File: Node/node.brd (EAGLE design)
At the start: 76.2 x 44.3 mm, 96 parts, among them CN4 MicroUSB, J1 U.FL, U1 MCP73871, U2 DW1000-I, U3 TPS61090RSAR, U4 ATMEGA328, X2 332-02, Y1 8MHz

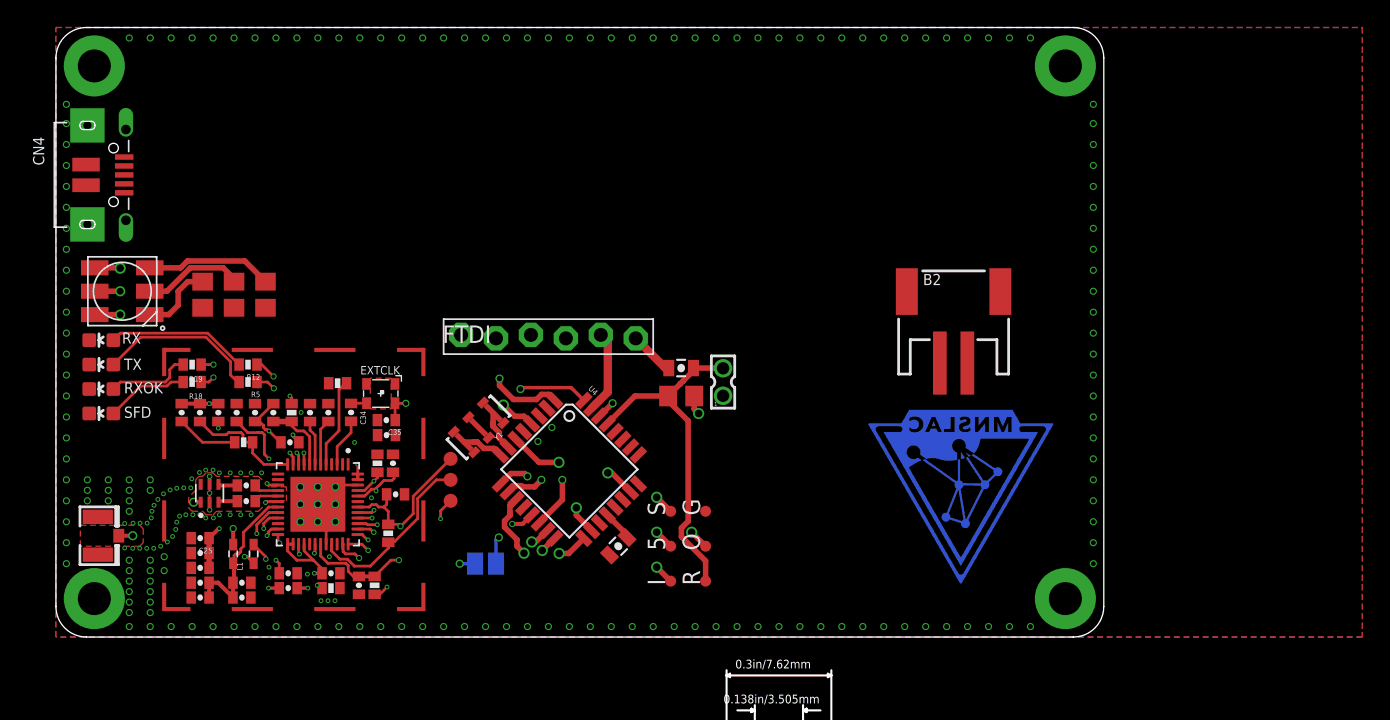
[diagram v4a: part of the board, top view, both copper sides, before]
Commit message: Added CP2105 FTDI chip
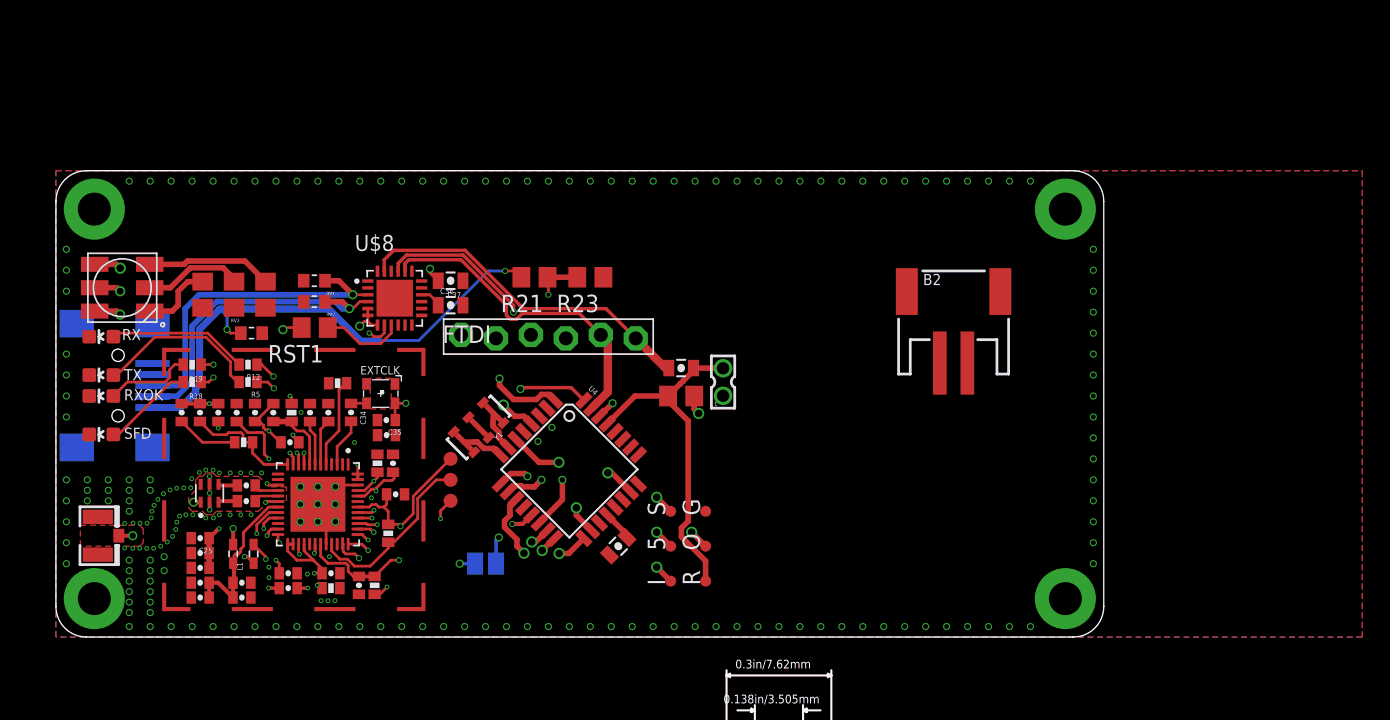
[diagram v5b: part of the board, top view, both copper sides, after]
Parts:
- removed CN4: MicroUSB, microbuilder:4UCONN_20329
- added C36: 4.7uF, SparkFun-Capacitors:0805-CAP
- added C37: 2uF, SparkFun-Capacitors:0805-CAP
- added J2: USBSMD, SparkFun-Connectors:USB-MINIB
- added R21: 24K, resistor:R0805
- added R23: 47K, resistor:R0805
- added RST1: 4.7K, resistor:R0805
- added RV1, RV2, RV3: WE-VE_0603_REFLOW, Wurth_Elektronik_Passive_rev15e:WESURGE_0603_REFLOW
- added U$8: CP2105, MainLib:QFN50P400X400X80-25N
- U$1: value MNSLAC0.25-EXP -> MNSLAC0.25; device MainLib:MNSLAC-0.25-EXPOSED -> MainLib:MNSLAC-0.25
- moved SFD 1.52 mm to (3.30, 14.7)
- moved TX 0.76 mm to (3.30, 19.1)
- moved RXOK 0.51 mm to (3.30, 17.5)
- moved RX 0.25 mm to (3.30, 21.8)
- moved LED1 0.25 mm to (4.83, 25.4)
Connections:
- new net D+: J2.D+, RV1.1, U$8.3
- new net D-: J2.D-, RV2.1, U$8.4
- new net N$19: RST1.1, U$8.9
- new net N$28: R21.1, R23.2, U$8.8
- new net N$29: C36.1, U$8.16
- net 3.3V: now also C37.2, RST1.2, U$8.5, U$8.6, U$8.7
- net DTR: now also U$8.23
- net GND: now also C36.2, C37.1, J2.GND, R23.1, RV1.2, RV2.2, RV3.2, U$8.2, U$8.25; no longer CN4.BASE@1, CN4.BASE@2, CN4.GND, CN4.SPRT@1, CN4.SPRT@2, CN4.SPRT@3, CN4.SPRT@4
- net RXD: now also U$8.21
- net TXD: now also U$8.20
- net VBUS: now also J2.VBUS, R21.2, RV3.1; no longer CN4.VBUS
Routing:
- net VBUS: track 0.00 -> 38.5 mm, vias 0 -> 2
- net D+: track 0.00 -> 23.8 mm, vias 0 -> 1
- net D-: track 0.00 -> 23.3 mm, vias 0 -> 1
- net DTR: track 3.30 -> 25.4 mm
- net N$28: track 0.00 -> 19.5 mm, vias 0 -> 2
- net TXD: track 6.03 -> 24.0 mm
- net RXD: track 8.57 -> 24.9 mm, vias 1 -> 2
- net N$19: track 0.00 -> 6.00 mm
- net 3.3V: track 25.0 -> 30.0 mm, vias 12 -> 15
- net N$29: track 0.00 -> 1.61 mm
- net N$21: track 6.02 -> 6.66 mm
- net GND: vias 232 -> 214
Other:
- board size 76.2 x 44.3 mm -> 76.2 x 33.9 mm

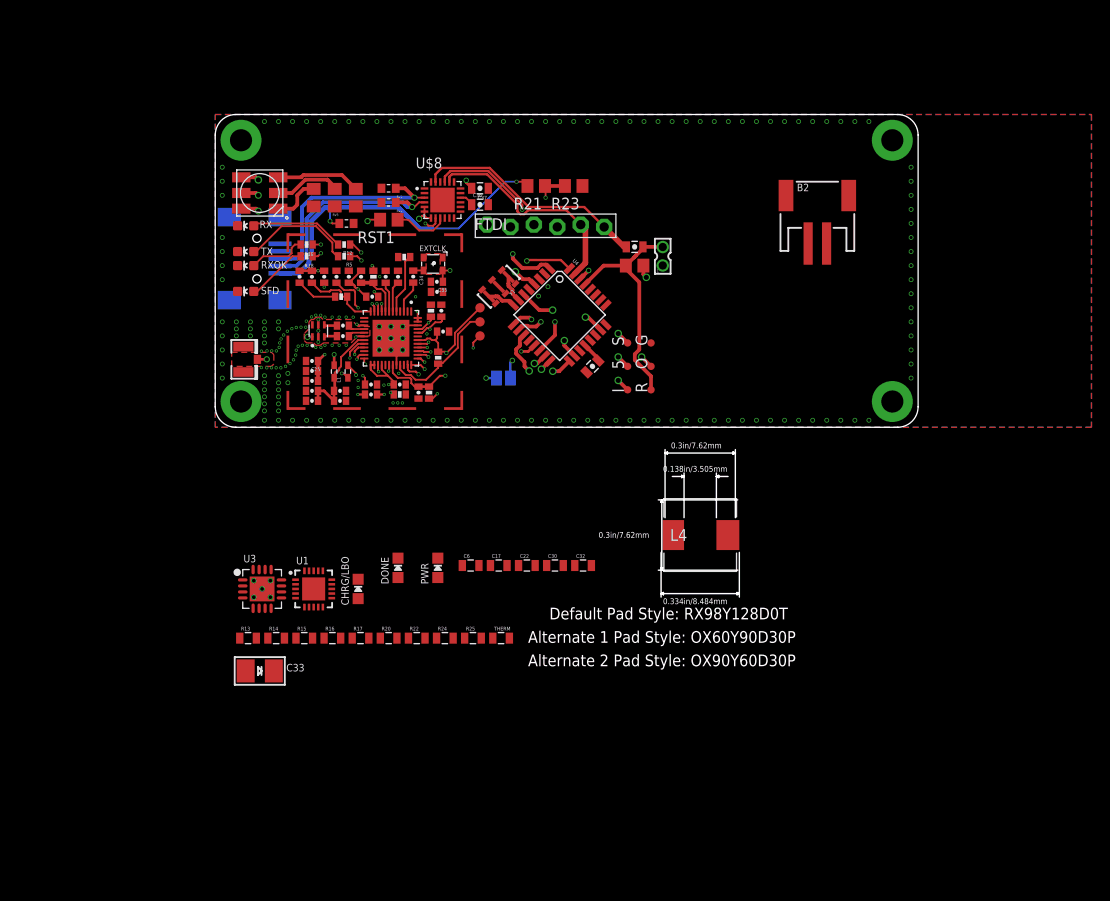
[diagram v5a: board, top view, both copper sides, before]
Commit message: Added sram chip, compass, buck/boost converter, lipo charger. DRC checks. Cosmetic changes.
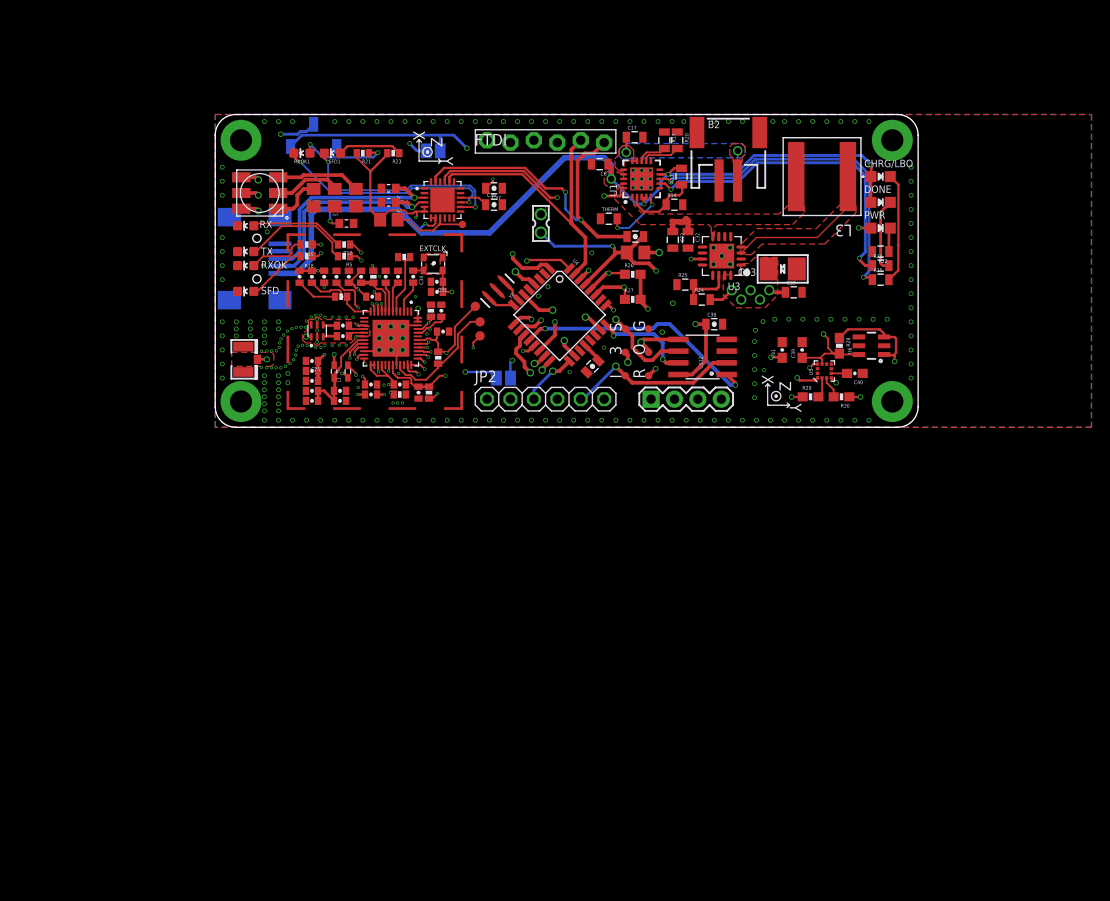
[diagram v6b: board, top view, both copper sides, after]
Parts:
- removed 5: TPSQTP08R, testpad:TP08R
- removed L4: https://www.digikey.com/product-detail/en/eaton-electronics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, MainLib:DR73
- removed Y1: 8MHz, SparkFun-FreqCtrl:RESONATOR-SMD_MED
- added 3, CPRST: TPSQTP08R, testpad:TP08R
- added C38: 1uF, SparkFun-Capacitors:0805-CAP
- added C39, C40, C41: 0.1uF, SparkFun-Capacitors:0603-CAP
- added JP1: (no value), SparkFun-Connectors:1X04
- added JP2: (no value), adafruit:1X06
- added L3: NR8040T6R8N, MainLib:IND_TAIYO_NR8040
- added R26, R27: 4.7K, SparkFun-Resistors:0603-RES
- added R28: 68, SparkFun-Passives:0603-RES
- added R29, R30: 10K, SparkFun-Resistors:0603-RES
- added RXOK1, SFD1: (no value), SparkFun-LED:LED-0603
- added SJ2: (no value), jumper:SJ
- added TP3: VDD_TP, SparkFun-Passives:TP_15TH
- added U$12: 23A640, MainLib:SOIC-8
- added U$15: SWITCH_SPDTJS102011JCQN, MainLib:JS102011JCQN
- added U5: LSM303C, SparkFun-DigitalIC:LGA-12
- added U6: LM3880, SparkFun-DigitalIC:SOT23-6
- added Y2: 8MHZ, SparkFun-FreqCtrl:RESONATOR-SMD
- R21: value 24K -> 470; device resistor:R0805 -> SparkFun-Passives:0402-RES
- R23: value 47K -> 470; device resistor:R0805 -> SparkFun-Passives:0402-RES
- moved R15 73.6 mm to (72.1, 16.0)
- moved CHRG/LBO 72.2 mm to (72.1, 27.2), turned to 270 degrees
- moved R16 71.9 mm to (72.1, 17.5)
- moved C33 71.5 mm to (61.5, 17.2), turned to 180 degrees
- moved R13 68.6 mm to (50.5, 27.2), turned to 90 degrees
- moved DONE 65.6 mm to (72.1, 24.4), turned to 270 degrees
- moved R22 65.5 mm to (72.1, 19.1), turned to 180 degrees
- moved R14 63.8 mm to (49.8, 24.1)
- moved R17 63.2 mm to (48.7, 31.1), turned to 270 degrees
- moved R20 62.4 mm to (50.1, 31.1), turned to 270 degrees
- moved U3 61.5 mm to (54.9, 18.6), turned to 180 degrees
- moved PWR 60.5 mm to (72.1, 21.6), turned to 270 degrees
- moved U1 56.9 mm to (46.2, 26.9), turned to 90 degrees
- moved C17 48.7 mm to (45.5, 31.4)
- moved THERM 46.9 mm to (42.7, 22.6)
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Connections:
- removed net A1: U4.24
- removed net A2: U4.25
- removed net D8: U4.12
- removed net VBAT: C22.1, C32.1, L4.1, U1.P$1, U1.P$20, U3.11, U3.8
- new net !CS_MAG: R30.2, U5.3
- new net !CS_XL: R29.2, U5.2
- new net !EXTCS: JP2.6, U4.25
- new net !SRAMCS: U$12.1, U4.12
- new net !SRAMHOLD: U$12.7, U4.24
- new net CPVIO: C37.2, R21.2, R23.2, RST1.2, U$8.5, U$8.6
- new net DRDY_MAG: U5.11
- new net N$30: SJ2.2, U$15.P$2, U3.11
- new net N$31: R21.1, RXOK1.A
- new net N$32: R23.1, SFD1.A
- new net RX_LED: SFD1.C, U$8.14
- new net TX_LED: RXOK1.C, U$8.15
- new net VCC-ISO: C22.1, C32.1, L3.2, SJ2.1, U$15.P$3, U1.P$1, U1.P$20, U3.8
- new net VDELAY: C39.1, R28.2, TP3.P$1, U5.9, U6.6
- net 3.3V: now also 3.TP, C38.1, C41.1, JP1.2, JP2.1, R26.2, R27.2, R28.1, R29.1, R30.1, U$12.8, U5.10, U6.1, U6.3; no longer 5.TP, C37.2, RST1.2, U$8.5, U$8.6, U$8.7
- net GND: now also C38.2, C39.2, C40.1, C41.2, JP1.1, JP2.2, U$12.4, U$15.P$1, U5.6, U5.8, U6.2, Y2.2; no longer R23.1, Y1.2
- net MISO: now also JP2.5, U$12.2
- net MOSI: now also JP2.4, U$12.5
- net N$1: now also Y2.3; no longer Y1.3
- net N$19: now also CPRST.TP
- net N$20: now also L3.1; no longer L4.2
- net N$28: now also C40.2, U5.5; no longer R21.1, R23.2, U$8.8
- net N$9: now also Y2.1; no longer Y1.1
- net SCK: now also JP2.3, U$12.6
- net SCL: now also JP1.4, R26.1, U5.1
- net SDA: now also JP1.3, R27.1, U5.4
- net VBUS: now also U$8.7, U$8.8; no longer R21.2
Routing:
- net N$30: track 0.00 -> 59.7 mm, vias 0 -> 3
- net VBUS: track 38.5 -> 95.6 mm, vias 2 -> 6
- net SDA: track 0.00 -> 46.8 mm, vias 0 -> 4
- net VCC-ISO: track 0.00 -> 45.9 mm, vias 0 -> 2
- net N$12: track 0.00 -> 37.1 mm, vias 0 -> 2
- net SCL: track 0.00 -> 35.6 mm, vias 0 -> 2
- net N$11: track 0.00 -> 35.4 mm, vias 0 -> 2
- net 3.3V: track 30.0 -> 62.7 mm, vias 15 -> 26
- net CPVIO: track 0.00 -> 29.1 mm, vias 0 -> 2
- net !SRAMCS: track 0.00 -> 27.4 mm, vias 0 -> 2
- net TX_LED: track 0.00 -> 24.0 mm, vias 0 -> 2
- net RX_LED: track 0.00 -> 23.3 mm, vias 0 -> 2
- net N$28: track 19.5 -> 1.70 mm, vias 2 -> 0
- net MISO: track 30.6 -> 48.0 mm
- net N$20: track 0.00 -> 16.9 mm
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- added copper zone on layer 1, net 3.3V
- added copper zone on layer 1, net N$20
- added copper zone on layer 1, net VBUS
- added copper zone on layer 1, net VCC-ISO
- added copper zone on layer 1, net VLIPO
- added copper zone on layer 16, net VLIPO
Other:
- board text added: "I2C"
- board text added: "P/U"
- board text added: "X"
- board text added: "Y"
- board text added: "Z"

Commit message: Created SAMD21 branch
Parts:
- added J3: CORTEX_DEBUGPTH, SparkFun-Connectors:2X5-PTH-1.27MM
- moved R28 0.10 mm to (67.7, 8.94)
- moved U6 0.08 mm to (71.1, 8.92)
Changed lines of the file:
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@@
 <attribute name="VALUE" x="70.358" y="6.985" size="0.4064" layer="27" font="vector" rot="R180"/>
 </element>
-<element name="R28" library="SparkFun-Passives" package="0603-RES" value="68" x="67.6656" y="8.8392" smashed="yes" rot="R270">
-<attribute name="NAME" x="68.4276" y="9.7282" size="0.4064" layer="25" font="vector" rot="R270"/>
-<attribute name="PROD_ID" value="RES-07860" x="67.6656" y="8.8392" size="1.778" layer="27" rot="R270" display="off"/>
-<attribute name="VALUE" x="66.5226" y="9.8552" size="0.4064" layer="27" font="vector" rot="R270"/>
+<element name="R28" library="SparkFun-Passives" package="0603-RES" value="68" x="67.6656" y="8.9408" smashed="yes" rot="R270">
+<attribute name="NAME" x="68.4276" y="9.8298" size="0.4064" layer="25" font="vector" rot="R270"/>
+<attribute name="PROD_ID" value="RES-07860" x="67.6656" y="8.9408" size="1.778" layer="27" rot="R270" display="off"/>
+<attribute name="VALUE" x="66.5226" y="9.9568" size="0.4064" layer="27" font="vector" rot="R270"/>
 </element>
-<element name="U6" library="SparkFun-DigitalIC" package="SOT23-6" value="LM3880" x="71.1454" y="8.8392" smashed="yes" rot="R90">
-<attribute name="NAME" x="68.9864" y="7.9502" size="0.4064" layer="25" rot="R90"/>
-<attribute name="PROD_ID" value="IC-12558" x="71.1454" y="8.8392" size="1.778" layer="27" rot="R90" display="off"/>
-<attribute name="VALUE" x="71.1359" y="7.7867" size="0.4064" layer="27" rot="R90"/>
+<element name="U6" library="SparkFun-DigitalIC" package="SOT23-6" value="LM3880" x="71.1454" y="8.9154" smashed="yes" rot="R90">
+<attribute name="NAME" x="68.9864" y="8.0264" size="0.4064" layer="25" rot="R90"/>
+<attribute name="PROD_ID" value="IC-12558" x="71.1454" y="8.9154" size="1.778" layer="27" rot="R90" display="off"/>
+<attribute name="VALUE" x="71.1359" y="7.8629" size="0.4064" layer="27" rot="R90"/>
 </element>
 <element name="C41" library="SparkFun-Capacitors" package="0603-CAP" value="0.1uF" x="61.468" y="8.382" smashed="yes" rot="R90">
@@
 <attribute name="PROD_ID" value="XTAL-08895" x="30.5816" y="14.8082" size="1.778" layer="27" rot="R225" display="off"/>
 <attribute name="VALUE" x="30.1325875" y="16.604253125" size="0.4064" layer="27" rot="R225"/>
+</element>
+<element name="J3" library="SparkFun-Connectors" package="2X5-PTH-1.27MM" value="CORTEX_DEBUGPTH" x="3.048" y="-3.048" smashed="yes">
+<attribute name="NAME" x="0" y="-1.651" size="0.8128" layer="25"/>
+<attribute name="VALUE" x="0.127" y="-4.445" size="0.8128" layer="27" align="top-left"/>
 </element>
 </elements>
@@
 <via x="58.5724" y="10.5156" extent="1-16" drill="0.35"/>
 <via x="58.4708" y="6.2484" extent="1-16" drill="0.35"/>
-<wire x1="66.29" y1="6.846" x2="66.79" y2="6.346" width="0" layer="19" extent="1-1"/>
 </signal>
 <signal name="DTR">
@@
 <contactref element="U6" pad="1"/>
 <contactref element="U5" pad="10"/>
-<wire x1="72.5205" y1="9.7892" x2="73.6244" y2="9.7892" width="0.254" layer="1"/>
-<wire x1="73.6244" y1="9.7892" x2="73.8124" y2="9.6012" width="0.254" layer="1"/>
+<wire x1="72.5205" y1="9.8654" x2="73.5482" y2="9.8654" width="0.254" layer="1"/>
+<wire x1="73.5482" y1="9.8654" x2="73.8124" y2="9.6012" width="0.254" layer="1"/>
 <wire x1="73.8124" y1="9.6012" x2="73.8124" y2="8.0772" width="0.254" layer="1"/>
 <wire x1="73.8124" y1="8.0772" x2="73.5584" y2="7.8232" width="0.254" layer="1"/>
-<wire x1="73.5584" y1="7.8232" x2="72.5865" y2="7.8232" width="0.254" layer="1"/>
-<wire x1="72.5865" y1="7.8232" x2="72.5205" y2="7.8892" width="0.254" layer="1"/>
-<wire x1="67.6656" y1="9.6892" x2="68.5936" y2="10.6172" width="0.254" layer="1"/>
-<wire x1="68.5936" y1="10.6172" x2="72.0344" y2="10.6172" width="0.254" layer="1"/>
+<wire x1="73.5584" y1="7.8232" x2="72.6627" y2="7.8232" width="0.254" layer="1"/>
+<wire x1="72.6627" y1="7.8232" x2="72.5205" y2="7.9654" width="0.254" layer="1"/>
+<wire x1="67.6656" y1="9.7908" x2="68.492" y2="10.6172" width="0.254" layer="1"/>
+<wire x1="68.492" y1="10.6172" x2="72.0344" y2="10.6172" width="0.254" layer="1"/>
 <wire x1="72.0344" y1="10.6172" x2="72.5205" y2="10.1311" width="0.254" layer="1"/>
-<wire x1="72.5205" y1="10.1311" x2="72.5205" y2="9.7892" width="0.254" layer="1"/>
+<wire x1="72.5205" y1="10.1311" x2="72.5205" y2="9.8654" width="0.254" layer="1"/>
 <via x="73.66" y="7.1374" extent="1-16" drill="0.4"/>
 <via x="62.484" y="3.2766" extent="1-16" drill="0.4"/>
@@
 <wire x1="65.786" y1="7.366" x2="65.62" y2="7.532" width="0.2032" layer="1"/>
 <wire x1="65.62" y1="7.532" x2="63.627" y2="7.532" width="0.2032" layer="1"/>
-<wire x1="67.564" y1="7.8876" x2="67.6656" y2="7.9892" width="0.2032" layer="1"/>
-<wire x1="69.7703" y1="7.8892" x2="67.7656" y2="7.8892" width="0.2032" layer="1"/>
-<wire x1="67.7656" y1="7.8892" x2="67.6656" y2="7.9892" width="0.2032" layer="1"/>
-<wire x1="67.6656" y1="7.9892" x2="67.1576" y2="7.9892" width="0.2032" layer="1"/>
+<wire x1="67.564" y1="7.9892" x2="67.6656" y2="8.0908" width="0.2032" layer="1"/>
+<wire x1="69.7703" y1="7.9654" x2="67.791" y2="7.9654" width="0.2032" layer="1"/>
+<wire x1="67.791" y1="7.9654" x2="67.6656" y2="8.0908" width="0.2032" layer="1"/>
+<wire x1="67.6656" y1="8.0908" x2="67.2592" y2="8.0908" width="0.2032" layer="1"/>
+<wire x1="67.2592" y1="8.0908" x2="67.1576" y2="7.9892" width="0.2032" layer="1"/>
 <wire x1="67.1576" y1="7.9892" x2="67.0424" y2="7.9892" width="0.2032" layer="1"/>
 <wire x1="67.0424" y1="7.9892" x2="66.4464" y2="8.5852" width="0.2032" layer="1"/>
